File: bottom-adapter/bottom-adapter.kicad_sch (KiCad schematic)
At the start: 17 parts, among them J2 Burn Wire

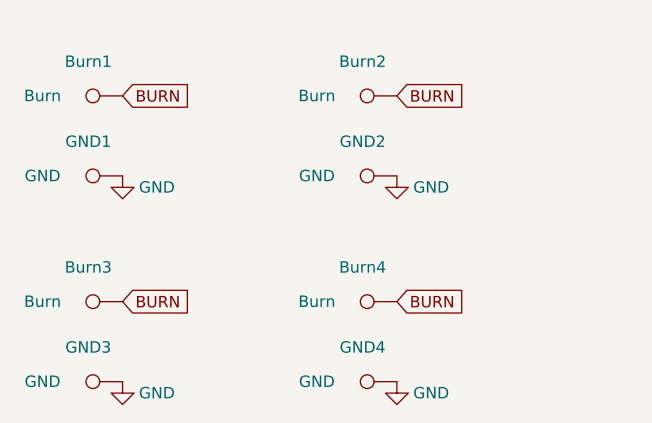
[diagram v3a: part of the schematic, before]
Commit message: new batt board and bottom adapter w/ fixed silkscreen
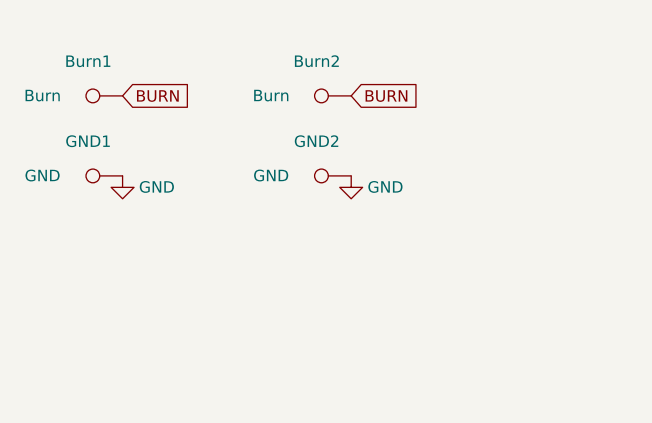
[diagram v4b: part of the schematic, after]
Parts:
- removed Burn2, Burn4: Burn, TestPoint:TestPoint_THTPad_2.0x2.0mm_Drill1.0mm, symbol Connector:TestPoint
- removed GND3, GND4: GND, TestPoint:TestPoint_THTPad_2.0x2.0mm_Drill1.0mm, symbol Connector:TestPoint
- renumbered Burn3 to Burn2
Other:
- moved on the sheet: Burn2, GND2
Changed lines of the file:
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@@
     )
   )
-  (global_label "BURN" (shape input) (at 48.26 73.66 0) (fields_autoplaced)
+  (global_label "BURN" (shape input) (at 73.66 50.8 0) (fields_autoplaced)
     (effects (font (size 1.27 1.27)) (justify left))
-    (property "Intersheet References" "${INTERSHEET_REFS}" (id 0) (at 55.8741 73.5806 0)
+    (property "Intersheet References" "${INTERSHEET_REFS}" (id 0) (at 81.2741 50.7206 0)
       (effects (font (size 1.27 1.27)) (justify left) hide)
     )
@@
     )
   )
-  (global_label "BURN" (shape input) (at 78.74 50.8 0) (fields_autoplaced)
-    (effects (font (size 1.27 1.27)) (justify left))
-    (property "Intersheet References" "${INTERSHEET_REFS}" (id 0) (at 86.3541 50.7206 0)
-      (effects (font (size 1.27 1.27)) (justify left) hide)
-    )
-  )
-  (global_label "BURN" (shape input) (at 78.74 73.66 0) (fields_autoplaced)
-    (effects (font (size 1.27 1.27)) (justify left))
-    (property "Intersheet References" "${INTERSHEET_REFS}" (id 0) (at 86.3541 73.5806 0)
-      (effects (font (size 1.27 1.27)) (justify left) hide)
-    )
-  )
-  (symbol (lib_id "Connector:TestPoint") (at 78.74 50.8 90) (unit 1)
-    (in_bom yes) (on_board yes)
-    (property "Reference" "Burn2" (id 0) (at 74.93 46.99 90))
-    (property "Value" "Burn" (id 1) (at 69.85 50.8 90))
-    (property "Footprint" "TestPoint:TestPoint_THTPad_2.0x2.0mm_Drill1.0mm" (id 2) (at 78.74 45.72 0)
-      (effects (font (size 1.27 1.27)) hide)
-    )
-    (property "Datasheet" "~" (id 3) (at 78.74 45.72 0)
-      (effects (font (size 1.27 1.27)) hide)
-    )
-    (pin "1")
-  )
   (symbol (lib_id "Connector:TestPoint") (at 48.26 50.8 90) (unit 1)
     (in_bom yes) (on_board yes)
@@
     (pin "1")
   )
-  (symbol (lib_id "Connector:TestPoint") (at 78.74 82.55 90) (unit 1)
-    (in_bom yes) (on_board yes)
-    (property "Reference" "GND4" (id 0) (at 74.93 78.74 90))
-    (property "Value" "GND" (id 1) (at 69.85 82.55 90))
-    (property "Footprint" "TestPoint:TestPoint_THTPad_2.0x2.0mm_Drill1.0mm" (id 2) (at 78.74 77.47 0)
-      (effects (font (size 1.27 1.27)) hide)
-    )
-    (property "Datasheet" "~" (id 3) (at 78.74 77.47 0)
-      (effects (font (size 1.27 1.27)) hide)
-    )
-    (pin "1")
-  )
-  (symbol (lib_id "Connector:TestPoint") (at 78.74 59.69 90) (unit 1)
-    (in_bom yes) (on_board yes)
-    (property "Reference" "GND2" (id 0) (at 74.93 55.88 90))
-    (property "Value" "GND" (id 1) (at 69.85 59.69 90))
-    (property "Footprint" "TestPoint:TestPoint_THTPad_2.0x2.0mm_Drill1.0mm" (id 2) (at 78.74 54.61 0)
-      (effects (font (size 1.27 1.27)) hide)
-    )
-    (property "Datasheet" "~" (id 3) (at 78.74 54.61 0)
+  (symbol (lib_id "Connector:TestPoint") (at 73.66 59.69 90) (unit 1)
+    (in_bom yes) (on_board yes)
+    (property "Reference" "GND2" (id 0) (at 69.85 55.88 90))
+    (property "Value" "GND" (id 1) (at 64.77 59.69 90))
+    (property "Footprint" "TestPoint:TestPoint_THTPad_2.0x2.0mm_Drill1.0mm" (id 2) (at 73.66 54.61 0)
+      (effects (font (size 1.27 1.27)) hide)
+    )
+    (property "Datasheet" "~" (id 3) (at 73.66 54.61 0)
       (effects (font (size 1.27 1.27)) hide)
     )
@@
     )
   )
-  (symbol (lib_id "Connector:TestPoint") (at 48.26 73.66 90) (unit 1)
-    (in_bom yes) (on_board yes)
-    (property "Reference" "Burn3" (id 0) (at 44.45 69.85 90))
-    (property "Value" "Burn" (id 1) (at 39.37 73.66 90))
-    (property "Footprint" "TestPoint:TestPoint_THTPad_2.0x2.0mm_Drill1.0mm" (id 2) (at 48.26 68.58 0)
-      (effects (font (size 1.27 1.27)) hide)
-    )
-    (property "Datasheet" "~" (id 3) (at 48.26 68.58 0)
+  (symbol (lib_id "Connector:TestPoint") (at 73.66 50.8 90) (unit 1)
+    (in_bom yes) (on_board yes)
+    (property "Reference" "Burn2" (id 0) (at 69.85 46.99 90))
+    (property "Value" "Burn" (id 1) (at 64.77 50.8 90))
+    (property "Footprint" "TestPoint:TestPoint_THTPad_2.0x2.0mm_Drill1.0mm" (id 2) (at 73.66 45.72 0)
+      (effects (font (size 1.27 1.27)) hide)
+    )
+    (property "Datasheet" "~" (id 3) (at 73.66 45.72 0)
       (effects (font (size 1.27 1.27)) hide)
     )
@@
     (pin "1")
   )
-  (symbol (lib_id "Connector:TestPoint") (at 48.26 82.55 90) (unit 1)
-    (in_bom yes) (on_board yes)
-    (property "Reference" "GND3" (id 0) (at 44.45 78.74 90))
-    (property "Value" "GND" (id 1) (at 39.37 82.55 90))
-    (property "Footprint" "TestPoint:TestPoint_THTPad_2.0x2.0mm_Drill1.0mm" (id 2) (at 48.26 77.47 0)
-      (effects (font (size 1.27 1.27)) hide)
-    )
-    (property "Datasheet" "~" (id 3) (at 48.26 77.47 0)
-      (effects (font (size 1.27 1.27)) hide)
-    )
-    (pin "1")
-  )
-  (symbol (lib_id "Connector:TestPoint") (at 78.74 73.66 90) (unit 1)
-    (in_bom yes) (on_board yes)
-    (property "Reference" "Burn4" (id 0) (at 74.93 69.85 90))
-    (property "Value" "Burn" (id 1) (at 69.85 73.66 90))
-    (property "Footprint" "TestPoint:TestPoint_THTPad_2.0x2.0mm_Drill1.0mm" (id 2) (at 78.74 68.58 0)
-      (effects (font (size 1.27 1.27)) hide)
-    )
-    (property "Datasheet" "~" (id 3) (at 78.74 68.58 0)
-      (effects (font (size 1.27 1.27)) hide)
-    )
-    (pin "1")
-  )
   (symbol (lib_id "Mechanical:MountingHole") (at 138.43 62.23 0) (unit 1)
     (in_bom yes) (on_board yes) (fields_autoplaced)
@@
     )
   )
-  (symbol (lib_id "power:GND") (at 48.26 82.55 0) (unit 1)
-    (in_bom yes) (on_board yes)
-    (property "Reference" "#PWR0102" (id 0) (at 48.26 88.9 0)
-      (effects (font (size 1.27 1.27)) hide)
-    )
-    (property "Value" "GND" (id 1) (at 52.07 83.82 0))
-    (property "Footprint" "" (id 2) (at 48.26 82.55 0)
-      (effects (font (size 1.27 1.27)) hide)
-    )
-    (property "Datasheet" "" (id 3) (at 48.26 82.55 0)
-      (effects (font (size 1.27 1.27)) hide)
-    )
-    (pin "1")
-  )
-  (symbol (lib_id "power:GND") (at 78.74 59.69 0) (unit 1)
-    (in_bom yes) (on_board yes)
-    (property "Reference" "#PWR0105" (id 0) (at 78.74 66.04 0)
-      (effects (font (size 1.27 1.27)) hide)
-    )
-    (property "Value" "GND" (id 1) (at 82.55 60.96 0))
-    (property "Footprint" "" (id 2) (at 78.74 59.69 0)
-      (effects (font (size 1.27 1.27)) hide)
-    )
-    (property "Datasheet" "" (id 3) (at 78.74 59.69 0)
+  (symbol (lib_id "power:GND") (at 73.66 59.69 0) (unit 1)
+    (in_bom yes) (on_board yes)
+    (property "Reference" "#PWR0105" (id 0) (at 73.66 66.04 0)
+      (effects (font (size 1.27 1.27)) hide)
+    )
+    (property "Value" "GND" (id 1) (at 77.47 60.96 0))
+    (property "Footprint" "" (id 2) (at 73.66 59.69 0)
+      (effects (font (size 1.27 1.27)) hide)
+    )
+    (property "Datasheet" "" (id 3) (at 73.66 59.69 0)
       (effects (font (size 1.27 1.27)) hide)
     )
@@
     )
   )
-  (symbol (lib_id "power:GND") (at 78.74 82.55 0) (unit 1)
-    (in_bom yes) (on_board yes)
-    (property "Reference" "#PWR0104" (id 0) (at 78.74 88.9 0)
-      (effects (font (size 1.27 1.27)) hide)
-    )
-    (property "Value" "GND" (id 1) (at 82.55 83.82 0))
-    (property "Footprint" "" (id 2) (at 78.74 82.55 0)
-      (effects (font (size 1.27 1.27)) hide)
-    )
-    (property "Datasheet" "" (id 3) (at 78.74 82.55 0)
-      (effects (font (size 1.27 1.27)) hide)
-    )
-    (pin "1")
-  )
   (sheet_instances
     (path "/" (page "1"))
   )
   (symbol_instances
-    (path "/ac35bc98-adc9-4e7c-b95f-38ae6c88db8a"
-      (reference "#PWR0102") (unit 1) (value "GND") (footprint "")
-    )
-    (path "/f870594d-5222-4d93-aa0e-6f8613145649"
-      (reference "#PWR0104") (unit 1) (value "GND") (footprint "")
-    )
     (path "/b088f046-9b33-457e-82ce-28efb69312be"
       (reference "#PWR0105") (unit 1) (value "GND") (footprint "")
@@
       (reference "Burn1") (unit 1) (value "Burn") (footprint "TestPoint:TestPoint_THTPad_2.0x2.0mm_Drill1.0mm")
     )
-    (path "/13d9b464-2493-4b50-b622-2bf59c0d3e7e"
+    (path "/7ff4347d-de77-468d-875e-d29c576dc06d"
       (reference "Burn2") (unit 1) (value "Burn") (footprint "TestPoint:TestPoint_THTPad_2.0x2.0mm_Drill1.0mm")
-    )
-    (path "/7ff4347d-de77-468d-875e-d29c576dc06d"
-      (reference "Burn3") (unit 1) (value "Burn") (footprint "TestPoint:TestPoint_THTPad_2.0x2.0mm_Drill1.0mm")
-    )
-    (path "/9e630d83-7edd-4afa-bf23-376812d8197b"
-      (reference "Burn4") (unit 1) (value "Burn") (footprint "TestPoint:TestPoint_THTPad_2.0x2.0mm_Drill1.0mm")
     )
     (path "/55db7b2e-06ee-4d8d-8af2-49e19af90dd2"
@@
       (reference "GND2") (unit 1) (value "GND") (footprint "TestPoint:TestPoint_THTPad_2.0x2.0mm_Drill1.0mm")
     )
-    (path "/9a265073-6bf2-45b0-8a22-73f2049dbd2c"
-      (reference "GND3") (unit 1) (value "GND") (footprint "TestPoint:TestPoint_THTPad_2.0x2.0mm_Drill1.0mm")
-    )
-    (path "/2c274c64-24e8-4763-9db7-22516d0251b3"
-      (reference "GND4") (unit 1) (value "GND") (footprint "TestPoint:TestPoint_THTPad_2.0x2.0mm_Drill1.0mm")
-    )
     (path "/e9946aa7-c9b6-4f3f-9c3f-ec0e16fd278b"
